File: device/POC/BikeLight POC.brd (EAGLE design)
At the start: 68.6 x 53.3 mm, 33 parts, among them IC1 MCP2515-I-ML, IC10 MCP1802T-5002I/OT, IC2 MICROSD_SPI_MODE, IC3 FM25W256-SOIC, IC4 MCP2561-2, IC5 TXB0106, IC6 PRQV8.00CR1510Y00L, IC7 ADXL345, IC8 74HCT1G32, IC9 MCP1802T-3302I/OT, X1 22-23-2021, X2 22-23-2021

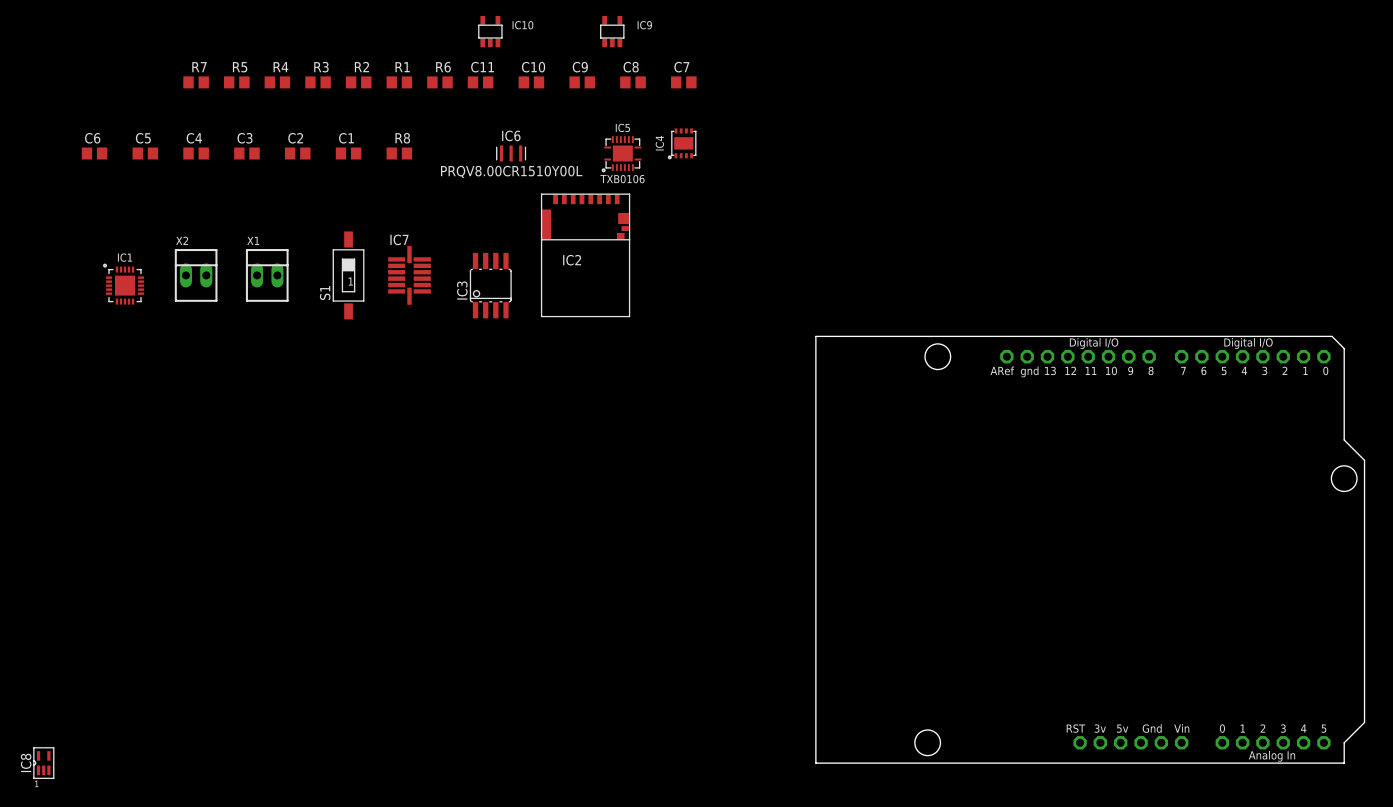
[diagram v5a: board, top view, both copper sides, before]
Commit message: - finshed layout - added LED to indicate power-on status - remapped most pins to better fit board layout - ERC/DRC report no errors
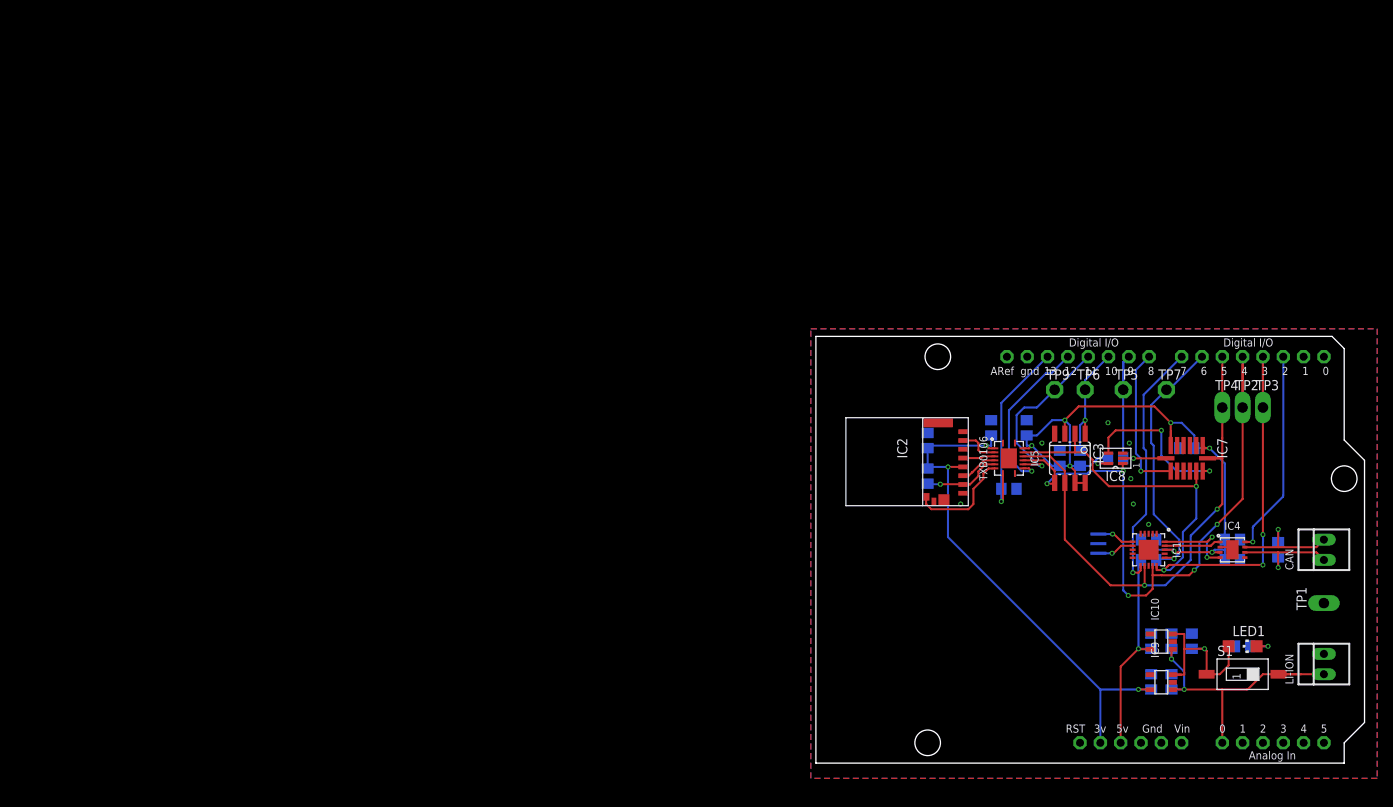
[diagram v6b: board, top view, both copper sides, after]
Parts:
- removed X1, X2: 22-23-2021, con-molex:22-23-2021
- added CAN, LI-ION: (no value), con-molex:22-23-2021
- added LED1: LTST-C230KSKT, led:CHIPLED_1206
- added R9: 10k, rcl:R0805
- added TP1, TP2, TP3, TP4: PTR1PAD1-13Y, testpad:P1-13Y
- added TP5, TP6, TP7, TP9: TPPAD1-13, testpad:P1-13
- moved IC8 139.3 mm to (37.5, 38.1), turned to 90 degrees
- moved C4 139.1 mm to (52.1, 25.4), flipped to the bottom, turned to 180 degrees
- moved R4 132.4 mm to (52.1, 27.9), flipped to the bottom, turned to 180 degrees
- moved IC1 132.1 mm to (41.6, 26.7), turned to 270 degrees
- moved R7 124.2 mm to (37.5, 38.1), flipped to the bottom, turned to 180 degrees
- moved S1 122.4 mm to (53.3, 11.1), turned to 270 degrees
- moved C6 121.5 mm to (26.4, 41.9), flipped to the bottom, turned to 90 degrees
- moved R6 120.0 mm to (57.8, 26.7), flipped to the bottom, turned to 90 degrees
- moved R8 116.3 mm to (47.0, 15.2), flipped to the bottom, turned to 270 degrees
- moved IC10 113.3 mm to (43.2, 15.2), turned to 90 degrees
- moved C5 111.1 mm to (21.9, 41.9), flipped to the bottom, turned to 90 degrees
- moved R1 111.1 mm to (41.6, 25.4), flipped to the bottom, turned to 180 degrees
- moved C1 111.0 mm to (41.6, 27.9), flipped to the bottom
- moved C11 109.1 mm to (41.9, 15.2), flipped to the bottom, turned to 90 degrees
- moved R5 109.1 mm to (24.1, 34.3), flipped to the bottom
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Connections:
- removed net P0.13-ADXL345_INT1_INTERRUPT_PIN: BRD1.D1, IC7.INT1
- removed net P0.14-: BRD1.D2
- removed net P0.15-MCP2515_INT: BRD1.D3, IC1.!INT!
- removed net P0.16-STBY: BRD1.D4, IC4.STBY, R4.2
- removed net P0.17-SD_CARD_DETECT: BRD1.D5, IC5.B6
- removed net P0.18-OE: BRD1.D6, IC5.OE, R5.2
- removed net P0.19-SPI_SS_ADXL345_PIN: BRD1.D7, IC7.!CS!, IC8.A, R7.2
- removed net P0.20-SPI_SS_SD-CARD: BRD1.D8, IC5.B5
- removed net P0.23-SPI_SS_FRAM: BRD1.D9, IC3.!CS!, R2.1
- removed net P0.24-SPI_SS_MCP2515: BRD1.D10, IC1.!CS!, R1.2
- removed net P0.25-SPI_MOSI: BRD1.D11, IC1.SI, IC3.SI, IC5.B4, IC8.B
- removed net P0.28-SPI_MISO: BRD1.D12, IC1.SO, IC3.SO, IC5.B2, IC7.SDO
- removed net P0.29-SPI_SCK: BRD1.D13, IC1.SCK, IC3.SCK, IC5.B3, IC7.SCL
- new net N$2: LED1.C, R9.1
- new net P0.13-: BRD1.D1
- new net P0.14-STBY: BRD1.D2, IC4.STBY, R4.2
- new net P0.15-SPI_MISO: BRD1.D3, IC1.SO, IC3.SO, IC5.B2, IC7.SDO, TP3.TP
- new net P0.16-SPI_MOSI: BRD1.D4, IC1.SI, IC3.SI, IC5.B4, IC8.B, TP2.TP
- new net P0.17-SPI_SCK: BRD1.D5, IC1.SCK, IC3.SCK, IC5.B3, IC7.SCL, TP4.TP
- new net P0.18-SPI_SS_MCP2515: BRD1.D6, IC1.!CS!, R1.2, TP7.TP
- new net P0.19-MCP2515_INT: BRD1.D7, IC1.!INT!
- new net P0.20-ADXL345_INT1_INTERRUPT_PIN: BRD1.D8, IC7.INT1
- new net P0.23-SPI_SS_ADXL345_PIN: BRD1.D9, IC7.!CS!, IC8.A, R7.2, TP5.TP
- new net P0.24-SPI_SS_FRAM: BRD1.D10, IC3.!CS!, R2.1, TP6.TP
- new net P0.25-SPI_SS_SD-CARD: BRD1.D11, IC5.B5, TP9.TP
- new net P0.28-SD_CARD_DETECT: BRD1.D12, IC5.B6
- new net P0.29-OE: BRD1.D13, IC5.OE, R5.2
- net !SNDN!: now also LED1.A
- net CANH: now also CAN.2; no longer X2.1
- net CANL: now also CAN.1; no longer X2.2
- net GND: now also LI-ION.2, R9.2, TP1.TP; no longer X1.2
- net P0.01-VLIION: now also LI-ION.1; no longer X1.1
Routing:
- net 5V0: track 0.00 -> 117.8 mm, vias 0 -> 9
- net P0.15-SPI_MISO: track 0.00 -> 89.0 mm, vias 0 -> 4
- net P0.16-SPI_MOSI: track 0.00 -> 81.2 mm, vias 0 -> 5
- net 3V3: track 0.00 -> 67.9 mm, vias 0 -> 3
- net P0.17-SPI_SCK: track 0.00 -> 66.8 mm, vias 0 -> 2
- net P0.01-VLIION: track 0.00 -> 38.0 mm, vias 0 -> 2
- net P0.18-SPI_SS_MCP2515: track 0.00 -> 33.3 mm, vias 0 -> 1
- net P0.19-MCP2515_INT: track 0.00 -> 31.4 mm, vias 0 -> 1
- net P0.14-STBY: track 0.00 -> 27.4 mm, vias 0 -> 1
- net P0.23-SPI_SS_ADXL345_PIN: track 0.00 -> 24.1 mm, vias 0 -> 1
- net P0.29-OE: track 0.00 -> 24.1 mm, vias 0 -> 1
- net P0.25-SPI_SS_SD-CARD: track 0.00 -> 22.3 mm, vias 0 -> 1
- net !SNDN!: track 0.00 -> 22.2 mm, vias 0 -> 1
- net P0.28-SD_CARD_DETECT: track 0.00 -> 20.9 mm, vias 0 -> 1
- net SDA: track 0.00 -> 19.8 mm, vias 0 -> 2
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- added copper zone on layer 1, net GND
- added copper zone on layer 16, net GND

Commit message: - finished layout (silk top and bottom) - created gerbers
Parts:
- removed TP5, TP6, TP7, TP9: TPPAD1-13, testpad:P1-13
- added CAN_GND: PTR1PAD1-13Y, testpad:P1-13Y
- added MISO, MOSI, SCK: (no value), testpad:P1-13Y
- TP1, TP2, TP3, TP4: value PTR1PAD1-13Y -> (none); device testpad:P1-13Y -> testpad:P1-13
- moved TP1 42.9 mm to (29.8, 46.7), turned to 0 degrees
- moved TP2 19.8 mm to (33.7, 46.7)
- moved TP3 17.6 mm to (38.4, 46.7)
- moved TP4 7.33 mm to (43.8, 46.7)
- renumbered S1 to POWER
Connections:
- net GND: now also CAN_GND.TP; no longer TP1.TP
- net P0.15-SPI_MISO: now also MISO.TP; no longer TP3.TP
- net P0.16-SPI_MOSI: now also MOSI.TP; no longer TP2.TP
- net P0.17-SPI_SCK: now also SCK.TP; no longer TP4.TP
- net P0.18-SPI_SS_MCP2515: now also TP4.TP; no longer TP7.TP
- net P0.23-SPI_SS_ADXL345_PIN: now also TP3.TP; no longer TP5.TP
- net P0.24-SPI_SS_FRAM: now also TP2.TP; no longer TP6.TP
- net P0.25-SPI_SS_SD-CARD: now also TP1.TP; no longer TP9.TP
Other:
- board text added: "+"
- board text added: "-"
- board text added: "BikeLight POC"
- board text added: "H"
- board text added: "L"
- board text added: "TP1 - SS SD CARD"
- board text added: "TP2 - SS FRAM"
- board text added: "TP3 - SS ADXL345"
- board text added: "TP4 - SS MCP2515"
- board text added: "ejovrh"
- board text added: "v.1"

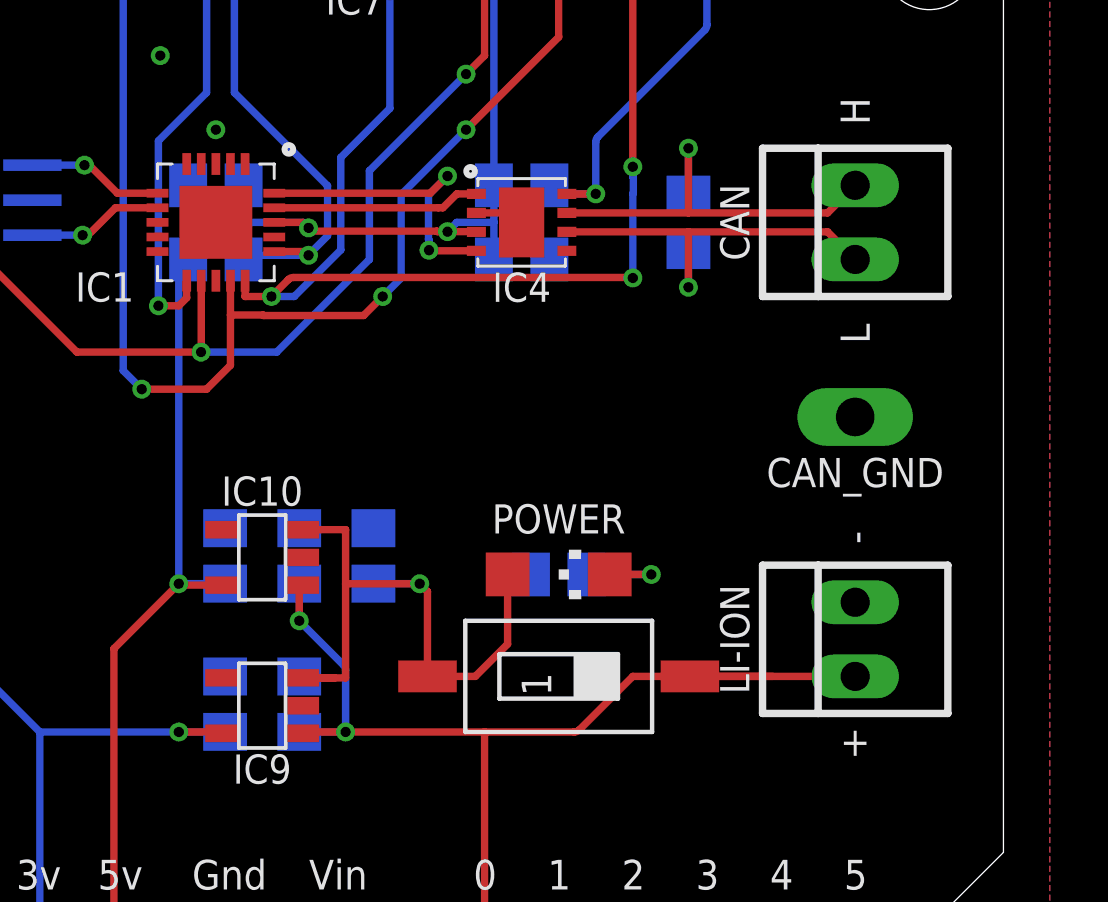
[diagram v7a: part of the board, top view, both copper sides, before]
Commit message: - decided to power the power indicator LED from 5V0 instead from the battery directly
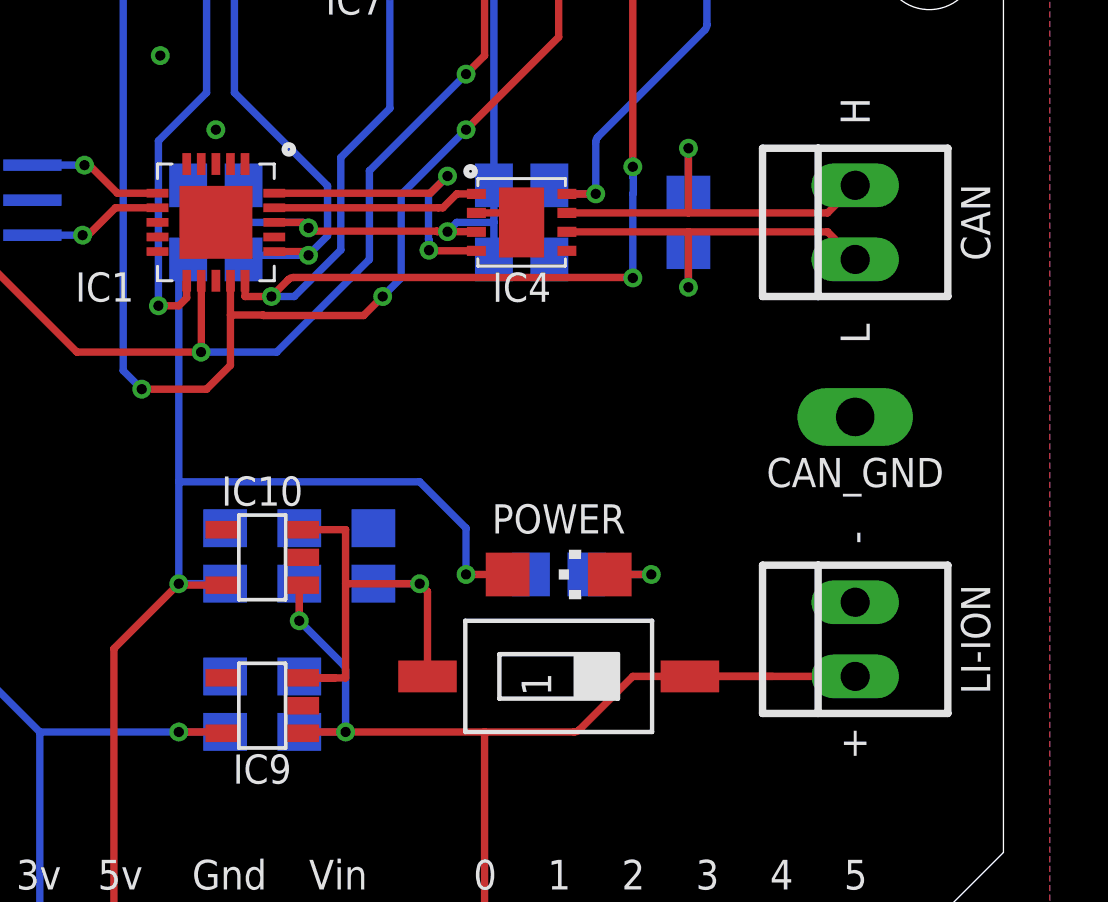
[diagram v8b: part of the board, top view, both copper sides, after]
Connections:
- net !SNDN!: no longer LED1.A
- net 5V0: now also LED1.A
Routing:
- net 5V0: track 117.8 -> 131.4 mm, vias 9 -> 10
- net !SNDN!: track 22.2 -> 16.6 mm
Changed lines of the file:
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@@
 <setting verticaltext="up"/>
 </settings>
-<grid distance="12.5" unitdist="mil" unit="mm" style="dots" multiple="1" display="yes" altdistance="5" altunitdist="mil" altunit="mil"/>
+<grid distance="12.5" unitdist="mil" unit="mil" style="dots" multiple="1" display="yes" altdistance="5" altunitdist="mil" altunit="mil"/>
 <layers>
 <layer number="1" name="Top" color="4" fill="1" visible="yes" active="yes"/>
@@
 <attribute name="MF" value="MOLEX" x="63.5" y="12.3825" size="1.778" layer="27" rot="R90" display="off"/>
 <attribute name="MPN" value="22-23-2021" x="63.5" y="12.3825" size="1.778" layer="27" rot="R90" display="off"/>
-<attribute name="NAME" x="59.3725" y="12.3825" size="1" layer="25" font="vector" rot="R90" align="center"/>
+<attribute name="NAME" x="67.6275" y="12.3825" size="1" layer="25" font="vector" rot="R90" align="center"/>
 <attribute name="OC_FARNELL" value="1462926" x="63.5" y="12.3825" size="1.778" layer="27" rot="R90" display="off"/>
 <attribute name="OC_NEWARK" value="25C3832" x="63.5" y="12.3825" size="1.778" layer="27" rot="R90" display="off"/>
@@
 <attribute name="MF" value="MOLEX" x="63.5" y="26.67" size="1.778" layer="27" rot="R90" display="off"/>
 <attribute name="MPN" value="22-23-2021" x="63.5" y="26.67" size="1.778" layer="27" rot="R90" display="off"/>
-<attribute name="NAME" x="59.3725" y="26.67" size="1" layer="25" font="vector" rot="R90" align="center"/>
+<attribute name="NAME" x="67.6275" y="26.67" size="1" layer="25" font="vector" rot="R90" align="center"/>
 <attribute name="OC_FARNELL" value="1462926" x="63.5" y="26.67" size="1.778" layer="27" rot="R90" display="off"/>
 <attribute name="OC_NEWARK" value="25C3832" x="63.5" y="26.67" size="1.778" layer="27" rot="R90" display="off"/>
@@
 <wire x1="44.577" y1="26.67" x2="42.545" y2="26.67" width="0.254" layer="16"/>
 <wire x1="40.3225" y1="25.08" x2="40.6425" y2="25.4" width="0.254" layer="16"/>
-<wire x1="40.3225" y1="14.2875" x2="40.3225" y2="25.08" width="0.254" layer="16"/>
+<wire x1="40.3225" y1="14.2875" x2="40.3225" y2="17.78" width="0.254" layer="16"/>
+<wire x1="40.3225" y1="17.78" x2="40.3225" y2="25.08" width="0.254" layer="16"/>
 <wire x1="42.3135" y1="44.5865" x2="44.355" y2="42.545" width="0.254" layer="1"/>
 <wire x1="32.839" y1="44.5865" x2="42.3135" y2="44.5865" width="0.254" layer="1"/>
@@
 <wire x1="35.2425" y1="37.465" x2="34.925" y2="37.7825" width="0.254" layer="16"/>
 <wire x1="40.3225" y1="14.2875" x2="38.1" y2="12.065" width="0.254" layer="1"/>
+<contactref element="LED1" pad="A"/>
+<wire x1="51.59" y1="14.605" x2="50.165" y2="14.605" width="0.254" layer="1"/>
+<via x="50.165" y="14.605" extent="1-16" drill="0.35"/>
+<wire x1="48.5775" y1="17.78" x2="50.165" y2="16.1925" width="0.254" layer="16"/>
+<wire x1="40.3225" y1="17.78" x2="48.5775" y2="17.78" width="0.254" layer="16"/>
+<wire x1="50.165" y1="16.1925" x2="50.165" y2="14.605" width="0.254" layer="16"/>
 </signal>
 <signal name="OSC1">
@@
 <wire x1="44.58" y1="11.06" x2="46.0375" y2="11.06" width="0.254" layer="1"/>
 <wire x1="48.7917" y1="11.06" x2="48.8442" y2="11.1125" width="0.254" layer="1"/>
-<contactref element="LED1" pad="A"/>
-<wire x1="51.59" y1="14.605" x2="51.59" y2="12.22" width="0.254" layer="1"/>
-<wire x1="51.59" y1="12.22" x2="50.4825" y2="11.1125" width="0.254" layer="1"/>
-<wire x1="50.4825" y1="11.1125" x2="48.8442" y2="11.1125" width="0.254" layer="1"/>
 <wire x1="48.5775" y1="14.2875" x2="46.0375" y2="14.2875" width="0.254" layer="1"/>
 </signal>
